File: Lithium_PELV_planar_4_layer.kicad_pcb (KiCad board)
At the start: 4 copper layers, 0 parts

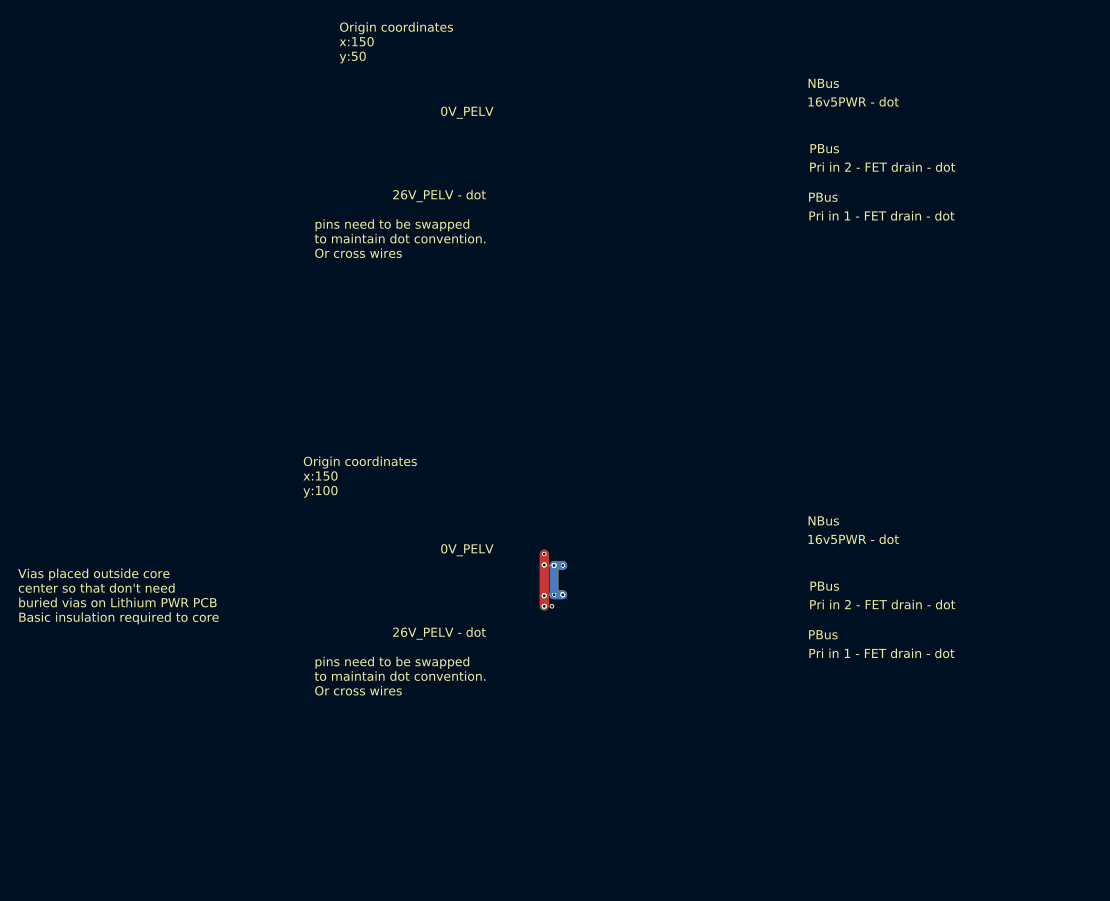
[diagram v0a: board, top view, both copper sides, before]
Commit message: Add 3D model folder and Samtec STEP
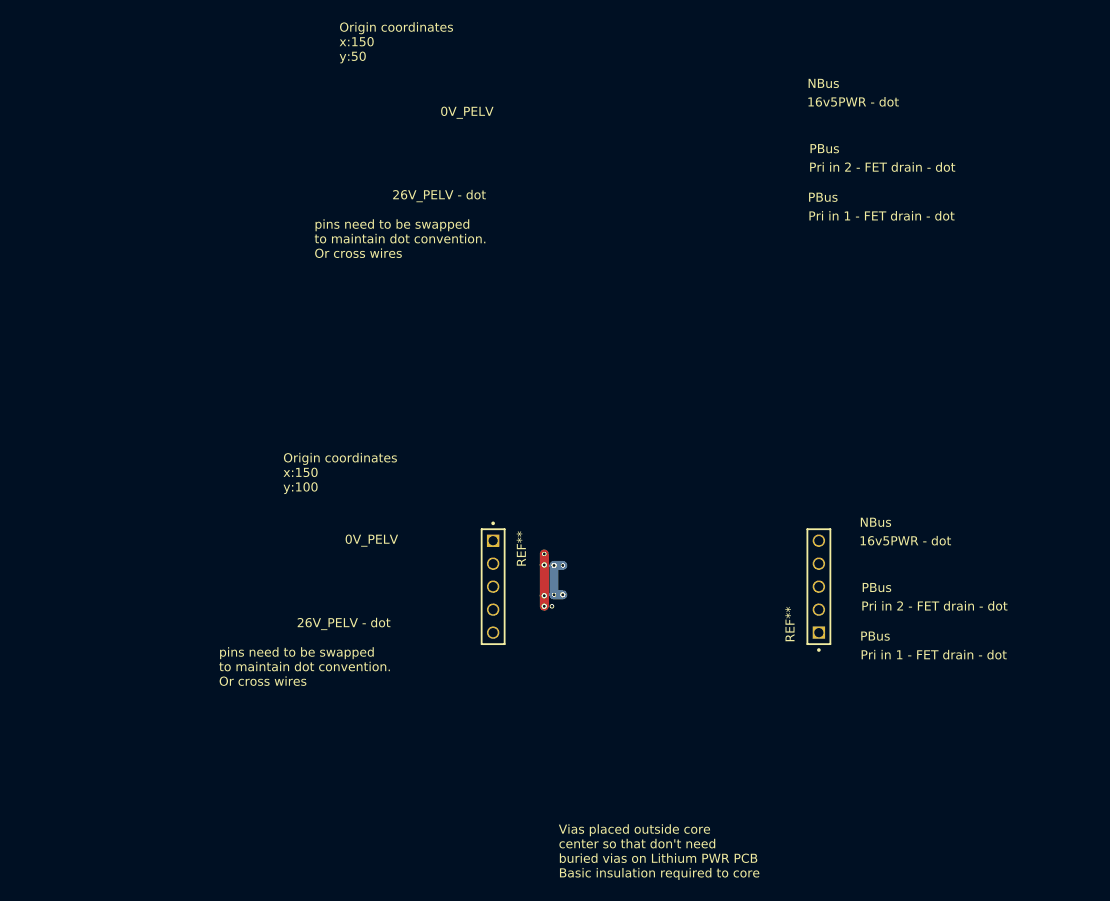
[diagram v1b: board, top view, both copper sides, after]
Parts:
- added REF**: SAMTEC_TSW-105-08-G-S, SAMTEC_TSW:SAMTEC_TSW-105-08-G-S, F.Cu at (132.0, 94.9)
- added REF**: SAMTEC_TSW-105-08-G-S, SAMTEC_TSW:SAMTEC_TSW-105-08-G-S, F.Cu at (168.0, 105.1)
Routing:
- net (no net): track 310.8 -> 261.2 mm
- net 26V_PELV: track 305.9 -> 355.5 mm
